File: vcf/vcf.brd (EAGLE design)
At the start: 88.9 x 107.6 mm, 96 parts, among them IC1 OPA4130U, IC2 OPA4130U, IC3 OPA4130U, IC4 OPA4130U, IC5 OPA4130U, Q1 BC847ASMD, Q2 BC847ASMD, Q3 BC847ASMD, Q4 BC847ASMD, Q5 BC847ASMD, Q6 BC847ASMD

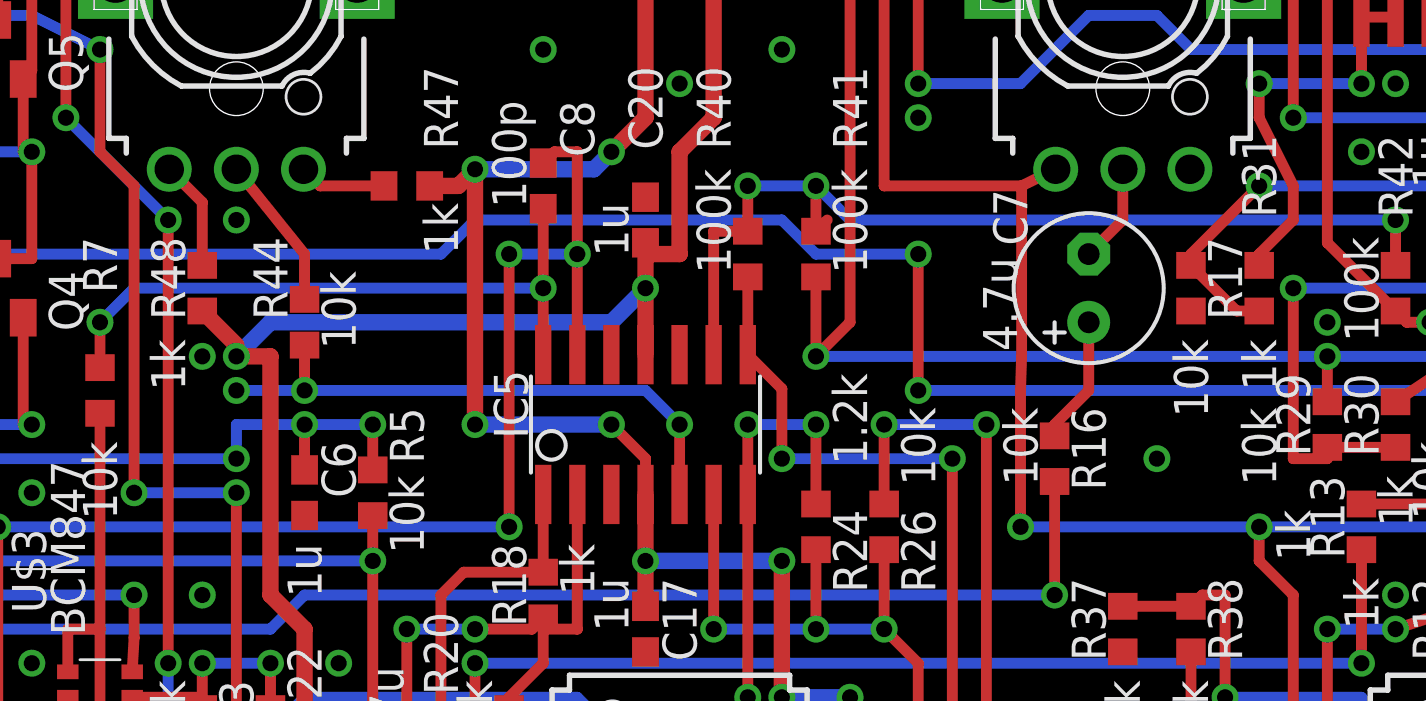
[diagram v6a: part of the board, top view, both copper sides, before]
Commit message: fixed polarity on resonance pot.  Sent out to fab.
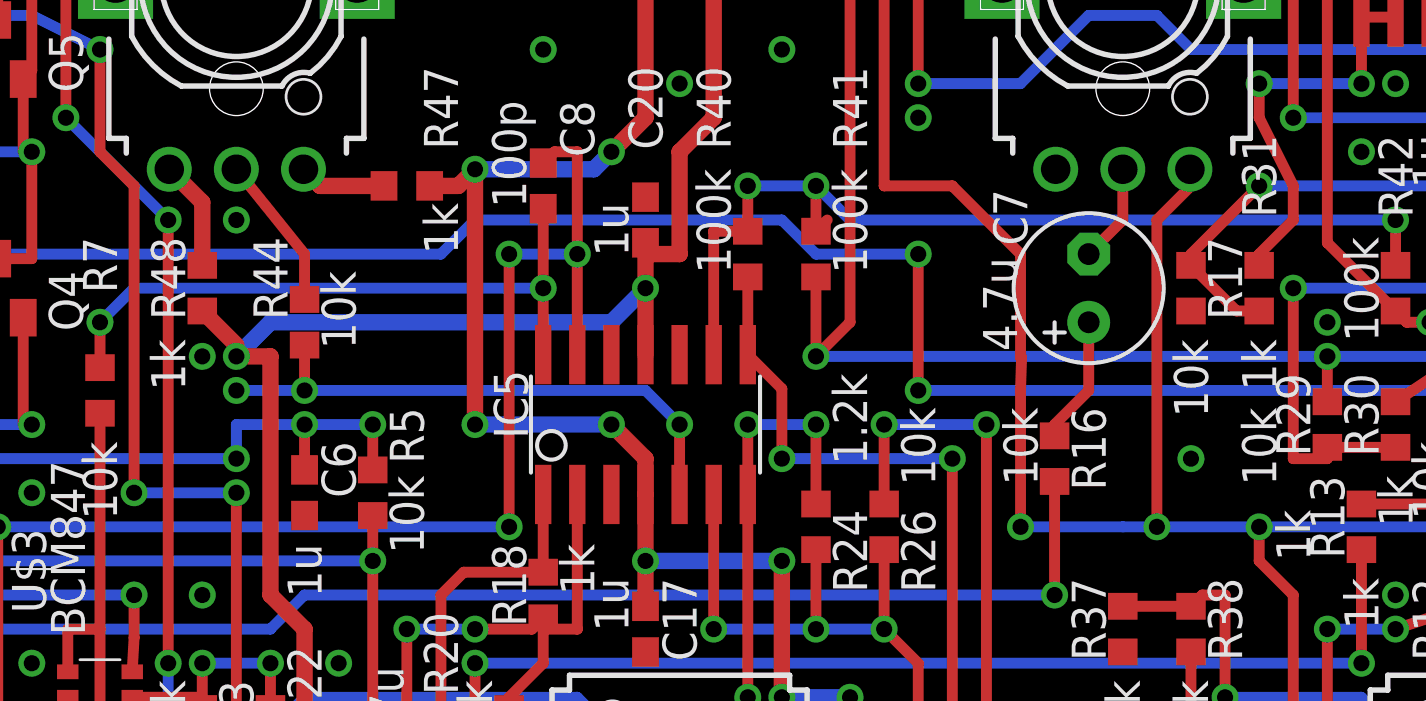
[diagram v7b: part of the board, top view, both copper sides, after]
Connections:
- net GND: now also Q.1; no longer Q.3
- net N$27: now also Q.3; no longer Q.1
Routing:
- net N$27: track 142.5 -> 153.4 mm, vias 8 -> 9
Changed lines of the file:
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@@
 <contactref element="C12" pad="2"/>
 <contactref element="XPAND" pad="9"/>
-<contactref element="Q" pad="3"/>
 <contactref element="GAIN" pad="1"/>
 <contactref element="GAIN1" pad="1"/>
@@
 <via x="58.42" y="50.8" extent="1-16" drill="0.6"/>
 <via x="58.42" y="55.88" extent="1-16" drill="0.6"/>
-<via x="62.23" y="66.04" extent="1-16" drill="0.6"/>
+<via x="63.5" y="66.04" extent="1-16" drill="0.6"/>
 <via x="48.26" y="81.28" extent="1-16" drill="0.6"/>
 <via x="39.37" y="81.28" extent="1-16" drill="0.6"/>
@@
 <via x="69.85" y="77.47" extent="1-16" drill="0.6"/>
 <via x="39.37" y="49.53" extent="1-16" drill="0.6"/>
+<contactref element="Q" pad="1"/>
 </signal>
 <signal name="N$16">
@@
 <wire x1="36.83" y1="67.31" x2="36.83" y2="76.82" width="0.6096" layer="1"/>
 <via x="36.83" y="76.82" extent="1-16" drill="0.6"/>
-<wire x1="43.18" y1="64.7065" x2="43.18" y2="66.04" width="0.4064" layer="1"/>
-<wire x1="43.18" y1="66.04" x2="41.91" y2="67.31" width="0.4064" layer="1"/>
+<wire x1="43.18" y1="64.7065" x2="43.18" y2="66.04" width="0.6096" layer="1"/>
+<wire x1="43.18" y1="66.04" x2="41.91" y2="67.31" width="0.6096" layer="1"/>
 <wire x1="50.8" y1="33.02" x2="50.8" y2="46.99" width="0.6096" layer="1"/>
 <wire x1="50.8" y1="46.99" x2="52.07" y2="48.26" width="0.6096" layer="1"/>
@@
 <contactref element="R15" pad="1"/>
 <contactref element="XPAND" pad="10"/>
-<contactref element="Q" pad="1"/>
 <contactref element="IC4" pad="1"/>
 <wire x1="76.2" y1="60.54" x2="76.2" y2="63.4365" width="0.4064" layer="1"/>
@@
 <via x="52.07" y="96.52" extent="1-16" drill="0.6"/>
 <wire x1="52.07" y1="96.52" x2="52.07" y2="76.2" width="0.4064" layer="1"/>
-<wire x1="52.07" y1="76.2" x2="57.19" y2="76.2" width="0.4064" layer="1"/>
-<wire x1="57.19" y1="76.2" x2="58.46" y2="76.82" width="0.4064" layer="1"/>
-<wire x1="57.19" y1="76.2" x2="57.19" y2="69.81" width="0.4064" layer="1"/>
 <wire x1="57.19" y1="69.81" x2="57.15" y2="68.58" width="0.4064" layer="1"/>
 <wire x1="57.15" y1="68.58" x2="57.15" y2="63.5" width="0.4064" layer="1"/>
 <via x="57.15" y="63.5" extent="1-16" drill="0.6"/>
-<wire x1="57.15" y1="63.5" x2="66.04" y2="63.5" width="0.4064" layer="16"/>
+<wire x1="57.15" y1="63.5" x2="60.96" y2="63.5" width="0.4064" layer="16"/>
 <via x="74.93" y="63.5" extent="1-16" drill="0.6"/>
+<wire x1="62.23" y1="63.5" x2="66.04" y2="63.5" width="0.4064" layer="16"/>
 <wire x1="66.04" y1="63.5" x2="74.93" y2="63.5" width="0.4064" layer="16"/>
 <wire x1="74.93" y1="63.5" x2="76.1365" y2="63.5" width="0.4064" layer="1"/>
@@
 <wire x1="66.04" y1="62.23" x2="66.04" y2="63.5" width="0.4064" layer="1"/>
 <contactref element="R46" pad="2"/>
+<contactref element="Q" pad="3"/>
+<wire x1="57.19" y1="69.81" x2="57.15" y2="69.81" width="0.4064" layer="1"/>
+<wire x1="57.15" y1="69.81" x2="57.15" y2="73.66" width="0.4064" layer="1"/>
+<wire x1="57.15" y1="73.66" x2="54.61" y2="76.2" width="0.4064" layer="1"/>
+<wire x1="54.61" y1="76.2" x2="52.07" y2="76.2" width="0.4064" layer="1"/>
+<wire x1="63.46" y1="76.82" x2="63.46" y2="76.16" width="0.4064" layer="1"/>
+<wire x1="63.46" y1="76.16" x2="62.23" y2="74.93" width="0.4064" layer="1"/>
+<wire x1="62.23" y1="74.93" x2="62.23" y2="63.5" width="0.4064" layer="1"/>
+<via x="62.23" y="63.5" extent="1-16" drill="0.6"/>
+<wire x1="62.23" y1="63.5" x2="60.96" y2="63.5" width="0.4064" layer="16"/>
 </signal>
 <signal name="N$15">
@@
 <wire x1="6.35" y1="13.97" x2="13.97" y2="13.97" width="0.4064" layer="16"/>
 </signal>
-<signal name="N$32">
-<contactref element="Q" pad="2"/>
-<contactref element="C7" pad="-"/>
-<wire x1="59.69" y1="73.66" x2="60.96" y2="74.93" width="0.4064" layer="1"/>
-<wire x1="60.96" y1="74.93" x2="60.96" y2="76.82" width="0.4064" layer="1"/>
-</signal>
 <signal name="N$57">
 <contactref element="GAIN" pad="2"/>
@@
 <contactref element="FREQ" pad="1"/>
 <contactref element="R48" pad="2"/>
-<wire x1="26.67" y1="73.24" x2="26.67" y2="75.59" width="0.4064" layer="1"/>
-<wire x1="26.67" y1="75.59" x2="25.44" y2="76.82" width="0.4064" layer="1"/>
+<wire x1="26.67" y1="73.24" x2="26.67" y2="75.59" width="0.6096" layer="1"/>
+<wire x1="26.67" y1="75.59" x2="25.44" y2="76.82" width="0.6096" layer="1"/>
 </signal>
 <signal name="N$66">
 <contactref element="FREQ" pad="3"/>
 <contactref element="R47" pad="1"/>
-<wire x1="33.44" y1="76.2" x2="31.06" y2="76.2" width="0.4064" layer="1"/>
-<wire x1="31.06" y1="76.2" x2="30.44" y2="76.82" width="0.4064" layer="1"/>
+<wire x1="33.44" y1="76.2" x2="31.06" y2="76.2" width="0.6096" layer="1"/>
+<wire x1="31.06" y1="76.2" x2="30.44" y2="76.82" width="0.6096" layer="1"/>
+</signal>
+<signal name="N$32">
+<contactref element="Q" pad="2"/>
+<contactref element="C7" pad="-"/>
+<wire x1="59.69" y1="73.66" x2="60.96" y2="74.93" width="0.4064" layer="1"/>
+<wire x1="60.96" y1="74.93" x2="60.96" y2="76.82" width="0.4064" layer="1"/>
 </signal>
 </signals>

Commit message: made some of the post first draft schematic changes
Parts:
- added R49, R50: 1k, dan:R0603
- R16: value 10k -> 1k
- R23: value 1k -> 100k
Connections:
- removed net N$65 (its old number): FREQ.1, R48.2
- new net N$60: FREQ.1, R47.1
- new net N$68: C6.1, R11.2, R49.1, R5.2, R50.2, R6.2
- net +12V: now also R50.1
- net N$13: now also R49.2; no longer C6.1, R11.2, R5.2, R6.2
- net N$66: now also R48.2; no longer R47.1
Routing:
- net N$13: track 52.8 -> 38.4 mm
- net N$65: track 5.74 -> 0.00 mm
- net N$65 (its old number): track 4.09 -> 0.00 mm
- net N$66: track 3.26 -> 0.00 mm
- net N$14: track 29.7 -> 28.0 mm
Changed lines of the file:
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@@
 <attribute name="VALUE" x="74.295" y="61.595" size="1.27" layer="21" font="vector" ratio="15" rot="R270"/>
 </element>
-<element name="R16" library="dan" package="R0603" value="10k" x="58.42" y="66.04" smashed="yes" rot="R90">
+<element name="R16" library="dan" package="R0603" value="1k" x="58.42" y="66.04" smashed="yes" rot="R90">
 <attribute name="NAME" x="59.055" y="67.945" size="1.27" layer="21" font="vector" ratio="15" rot="R270"/>
 <attribute name="VALUE" x="56.515" y="67.945" size="1.27" layer="21" font="vector" ratio="15" rot="R270"/>
@@
 <attribute name="VALUE" x="29.845" y="55.245" size="1.27" layer="21" font="vector" ratio="15" rot="R270"/>
 </element>
-<element name="R23" library="dan" package="R0603" value="1k" x="26.67" y="55.88" smashed="yes" rot="R90">
+<element name="R23" library="dan" package="R0603" value="100k" x="26.67" y="55.88" smashed="yes" rot="R90">
 <attribute name="NAME" x="27.305" y="57.785" size="1.27" layer="21" font="vector" ratio="15" rot="R270"/>
 <attribute name="VALUE" x="24.765" y="57.785" size="1.27" layer="21" font="vector" ratio="15" rot="R270"/>
@@
 <attribute name="VALUE" x="24.765" y="70.485" size="1.27" layer="21" font="vector" ratio="15" rot="R270"/>
 </element>
+<element name="R49" library="dan" package="R0603" value="1k" x="-5.08" y="-6.35"/>
+<element name="R50" library="dan" package="R0603" value="1k" x="-5.08" y="-11.43"/>
 </elements>
 <signals>
@@
 <contactref element="R4" pad="1"/>
 <contactref element="Q4" pad="1"/>
-<contactref element="R6" pad="2"/>
-<contactref element="R5" pad="2"/>
-<contactref element="C6" pad="1"/>
-<contactref element="R11" pad="2"/>
-<wire x1="5.08" y1="71.54" x2="5.08" y2="63.08" width="0.4064" layer="1"/>
 <wire x1="7.94" y1="71.29" x2="5.08" y2="71.29" width="0.4064" layer="1"/>
 <wire x1="5.08" y1="71.29" x2="5.08" y2="71.54" width="0.4064" layer="1"/>
-<wire x1="7.62" y1="63.08" x2="5.08" y2="63.08" width="0.4064" layer="1"/>
 <wire x1="7.94" y1="71.29" x2="7.62" y2="71.29" width="0.4064" layer="1"/>
 <wire x1="7.62" y1="71.29" x2="7.62" y2="68.58" width="0.4064" layer="1"/>
@@
 <wire x1="17.78" y1="66.04" x2="27.94" y2="66.04" width="0.4064" layer="16"/>
 <via x="27.94" y="66.04" extent="1-16" drill="0.6"/>
-<wire x1="30.48" y1="65.62" x2="30.48" y2="67.31" width="0.4064" layer="1"/>
 <via x="30.48" y="67.31" extent="1-16" drill="0.6"/>
 <wire x1="30.48" y1="67.31" x2="27.94" y2="67.31" width="0.4064" layer="16"/>
 <wire x1="27.94" y1="67.31" x2="27.94" y2="66.04" width="0.4064" layer="16"/>
-<wire x1="33.02" y1="65.62" x2="33.02" y2="67.31" width="0.4064" layer="1"/>
 <via x="33.02" y="67.31" extent="1-16" drill="0.6"/>
 <wire x1="33.02" y1="67.31" x2="30.48" y2="67.31" width="0.4064" layer="16"/>
+<contactref element="R49" pad="2"/>
+<wire x1="-4.23" y1="-6.35" x2="17.78" y2="66.04" width="0" layer="19" extent="1-16"/>
 </signal>
 <signal name="N$14">
 <contactref element="U$1" pad="2"/>
-<contactref element="R5" pad="1"/>
 <contactref element="C5" pad="+"/>
 <wire x1="33.02" y1="52.07" x2="33.02" y2="62.23" width="0.4064" layer="1"/>
-<wire x1="33.02" y1="62.23" x2="33.02" y2="63.92" width="0.4064" layer="1"/>
 <wire x1="15.17" y1="62.23" x2="17.78" y2="62.23" width="0.4064" layer="1"/>
 <via x="17.78" y="62.23" extent="1-16" drill="0.6"/>
 <wire x1="17.78" y1="62.23" x2="33.02" y2="62.23" width="0.4064" layer="16"/>
 <via x="33.02" y="62.23" extent="1-16" drill="0.6"/>
+<contactref element="R5" pad="1"/>
+<wire x1="33.02" y1="62.23" x2="33.02" y2="63.92" width="0" layer="19" extent="1-1"/>
 </signal>
 <signal name="GND">
@@
 <wire x1="35.14" y1="76.2" x2="36.21" y2="76.2" width="0.6096" layer="1"/>
 <wire x1="36.21" y1="76.2" x2="36.83" y2="76.82" width="0.6096" layer="1"/>
+<contactref element="R50" pad="1"/>
+<wire x1="-5.93" y1="-11.43" x2="21.59" y2="30.48" width="0" layer="19" extent="1-1"/>
 </signal>
 <signal name="-12V">
@@
 <wire x1="71.54" y1="34.29" x2="69.85" y2="34.29" width="0.4064" layer="1"/>
 </signal>
-<signal name="N$60">
-<contactref element="FREQ" pad="2"/>
-<contactref element="R44" pad="1"/>
-<wire x1="27.94" y1="76.82" x2="30.48" y2="73.66" width="0.4064" layer="1"/>
-<wire x1="30.48" y1="73.66" x2="30.48" y2="71.97" width="0.4064" layer="1"/>
-</signal>
 <signal name="N$62">
 <contactref element="R20" pad="1"/>
@@
 <wire x1="82.55" y1="13.97" x2="74.93" y2="13.97" width="0.4064" layer="16"/>
 </signal>
-<signal name="N$65">
-<contactref element="FREQ" pad="1"/>
-<contactref element="R48" pad="2"/>
-<wire x1="26.67" y1="73.24" x2="26.67" y2="75.59" width="0.6096" layer="1"/>
-<wire x1="26.67" y1="75.59" x2="25.44" y2="76.82" width="0.6096" layer="1"/>
-</signal>
-<signal name="N$66">
-<contactref element="FREQ" pad="3"/>
-<contactref element="R47" pad="1"/>
-<wire x1="33.44" y1="76.2" x2="31.06" y2="76.2" width="0.6096" layer="1"/>
-<wire x1="31.06" y1="76.2" x2="30.44" y2="76.82" width="0.6096" layer="1"/>
-</signal>
 <signal name="N$32">
 <contactref element="Q" pad="2"/>
@@
 <wire x1="60.96" y1="74.93" x2="60.96" y2="76.82" width="0.4064" layer="1"/>
 </signal>
+<signal name="N$68">
+<contactref element="R49" pad="1"/>
+<contactref element="R5" pad="2"/>
+<contactref element="C6" pad="1"/>
+<contactref element="R11" pad="2"/>
+<contactref element="R6" pad="2"/>
+<contactref element="R50" pad="2"/>
+<wire x1="30.48" y1="65.62" x2="33.02" y2="65.62" width="0" layer="19" extent="1-1"/>
+<wire x1="7.62" y1="63.08" x2="30.48" y2="65.62" width="0" layer="19" extent="1-1"/>
+<wire x1="5.08" y1="63.08" x2="7.62" y2="63.08" width="0" layer="19" extent="1-1"/>
+<wire x1="-5.93" y1="-6.35" x2="5.08" y2="63.08" width="0" layer="19" extent="1-1"/>
+<wire x1="-4.23" y1="-11.43" x2="-5.93" y2="-6.35" width="0" layer="19" extent="1-1"/>
+</signal>
+<signal name="N$60">
+<contactref element="FREQ" pad="1"/>
+<contactref element="R47" pad="1"/>
+<wire x1="25.44" y1="76.82" x2="33.44" y2="76.2" width="0" layer="19" extent="1-1"/>
+</signal>
+<signal name="N$65">
+<contactref element="FREQ" pad="2"/>
+<contactref element="R44" pad="1"/>
+<wire x1="30.48" y1="71.97" x2="27.94" y2="76.82" width="0" layer="19" extent="1-1"/>
+</signal>
+<signal name="N$66">
+<contactref element="FREQ" pad="3"/>
+<contactref element="R48" pad="2"/>
+<wire x1="26.67" y1="73.24" x2="30.44" y2="76.82" width="0" layer="19" extent="1-1"/>
+</signal>
 </signals>
